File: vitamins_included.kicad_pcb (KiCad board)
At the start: 2 copper layers, 230.5 x 82 mm, 130 parts, among them J1 Speaker, J3 ISP, J5 Speaker, J6 ISP, J7 WS2812>, J8 WS2812>, P2 UJ2-MBH-1-SMT, P3 >WS2812, P4 SJ-43514-SMT, P5 UJ2-MBH-1-SMT, P6 >WS2812, P8 SJ-43514-SMT, SW1 Socket, SW10 Socket, SW11 Socket, SW12 Socket, SW13 Socket, SW14 Socket, SW15 Socket, SW16 Socket, SW17 Socket, SW18 Socket, SW19 Socket, SW2 Socket, SW20 Socket, SW21 Socket, SW22 Socket, SW23 Socket, SW24 Socket, SW24 Socket-overlap, SW25 Socket, SW26 Socket, SW27 Socket, SW28 Socket, SW29 Socket, SW3 Socket, SW30 Socket, SW31 Socket, SW32 Socket, SW33 Socket, SW34 Socket, SW35 Socket, SW36 Socket, SW37 Socket, SW38 Socket, SW39 Socket, SW4 Socket, SW40 Socket, SW41 Socket, SW42 Socket, SW43 Socket, SW43 Socket-overlap, SW44 Socket, SW45 Socket, SW46 Socket, SW47 Socket, SW48 Socket, SW5 Socket, SW6 Socket, SW7 Socket, SW8 Socket, SW9 Socket, U1 ATMega32U4, U2 ATMega32U4, Y1 16MHz, Y2 16MHz

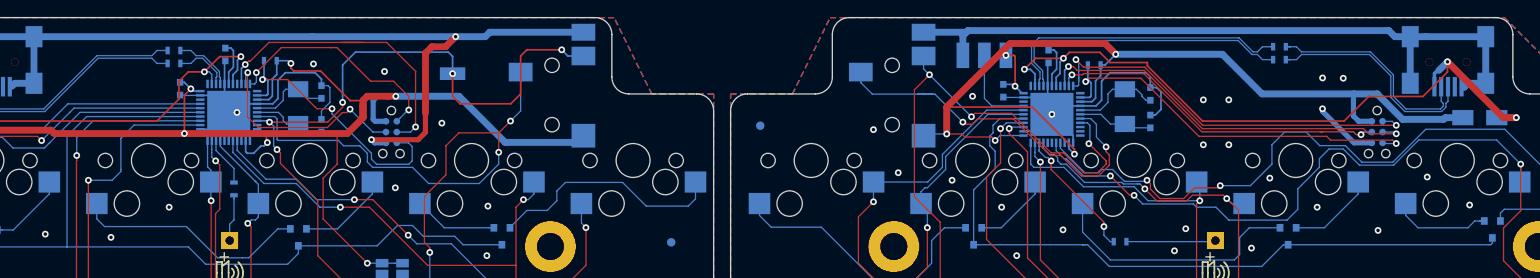
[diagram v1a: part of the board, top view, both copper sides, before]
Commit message: Added resistors to allow MCU to determin which half it is on
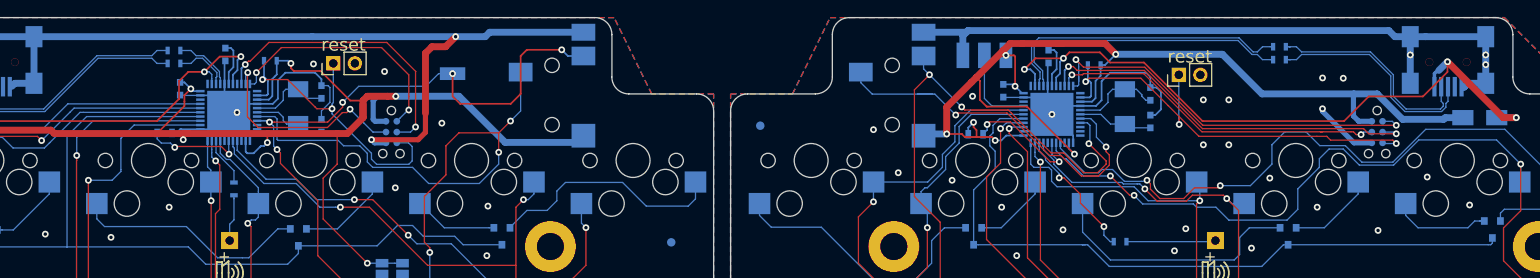
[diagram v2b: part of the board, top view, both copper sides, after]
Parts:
- added J2: reset, Connector_PinHeader_2.54mm:PinHeader_1x02_P2.54mm_Vertical, F.Cu at (69.4, 5.40)
- added J4: reset, Connector_PinHeader_2.54mm:PinHeader_1x02_P2.54mm_Vertical, F.Cu at (169.1, 6.75)
- added R11: 4k7, Resistor_SMD:R_0603_1608Metric, B.Cu at (49.5, 13.6)
- added R12: 4k7, Resistor_SMD:R_0603_1608Metric, B.Cu at (145.2, 13.8)
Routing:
- net Net-(R12-Pad1): track 0.00 -> 14.5 mm, vias 0 -> 2
- net Net-(R11-Pad1): track 0.00 -> 11.6 mm, vias 0 -> 2
- net /Right half/~RESET: track 47.5 -> 54.2 mm, vias 2 -> 3
- net /Left half/SDA: track 84.7 -> 78.8 mm
- net /Left half/~Reset: track 32.3 -> 37.7 mm
- net GND: track 302.5 -> 306.0 mm, vias 50 -> 53
- net /Left half/MISO: track 27.2 -> 28.7 mm
- net VCC: track 306.9 -> 305.7 mm, vias 14 -> 15
- net /Right half/col1: track 76.5 -> 77.6 mm
- net /Right half/col0: track 98.8 -> 99.9 mm
- net /Right half/col2: track 91.6 -> 92.3 mm
- net /Right half/buzz: track 16.6 -> 16.0 mm

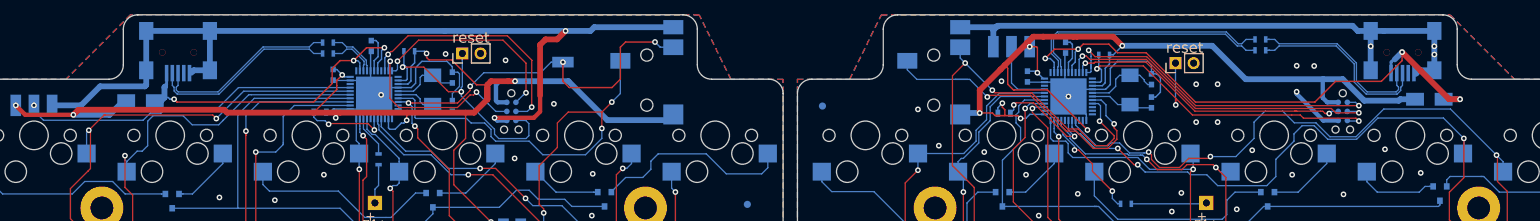
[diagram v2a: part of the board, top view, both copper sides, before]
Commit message: Changed to USB-C connector
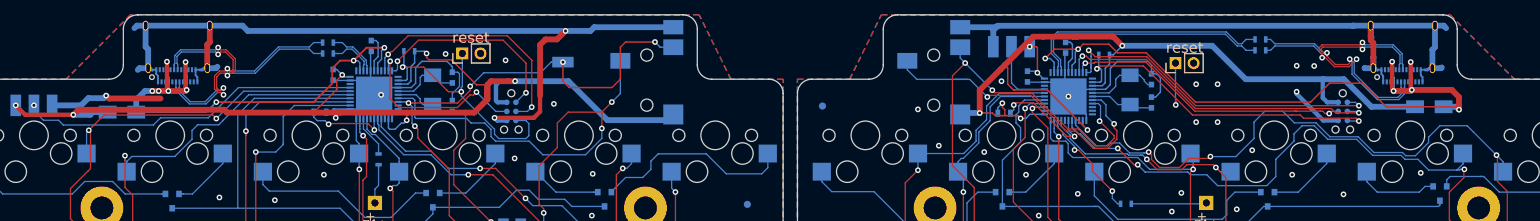
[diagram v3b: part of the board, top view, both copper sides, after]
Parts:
- removed P2, P5: UJ2-MBH-1-SMT, Connectors:USB-Mini-B-SMD
- added J10: 12401598E4#2A, Connector_USB:USB_C_Receptacle_Amphenol_12401610E4-2A, B.Cu at (200.9, 4.35)
- added J9: 12401598E4#2A, Connector_USB:USB_C_Receptacle_Amphenol_12401610E4-2A, B.Cu at (29.6, 4.35)
- R3: value 200R -> 220R
- moved D25 3.05 mm to (21.8, 13.6)
- moved D26 1.05 mm to (204.6, 12.8)
- moved G*** 0.40 mm to (44.1, 6.75)
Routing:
- net VBUS: track 127.6 -> 173.5 mm, vias 7 -> 16
- net GND: track 306.0 -> 328.4 mm, vias 53 -> 50
- net /Left half/Dd+: track 25.9 -> 43.2 mm, vias 0 -> 3
- net /Right half/Dd+: track 26.3 -> 43.3 mm, vias 0 -> 3
- net /Left half/Dd-: track 26.4 -> 43.2 mm, vias 0 -> 3
- net /Right half/Dd-: track 25.8 -> 42.3 mm, vias 0 -> 3
- net /Right half/col4: track 139.7 -> 135.5 mm
- net VCC: track 305.7 -> 302.7 mm
- net /Left half/col1: track 108.2 -> 105.9 mm
- net /Right half/col5: track 140.3 -> 141.0 mm
- net /Left half/wd2812-in: track 47.4 -> 48.0 mm

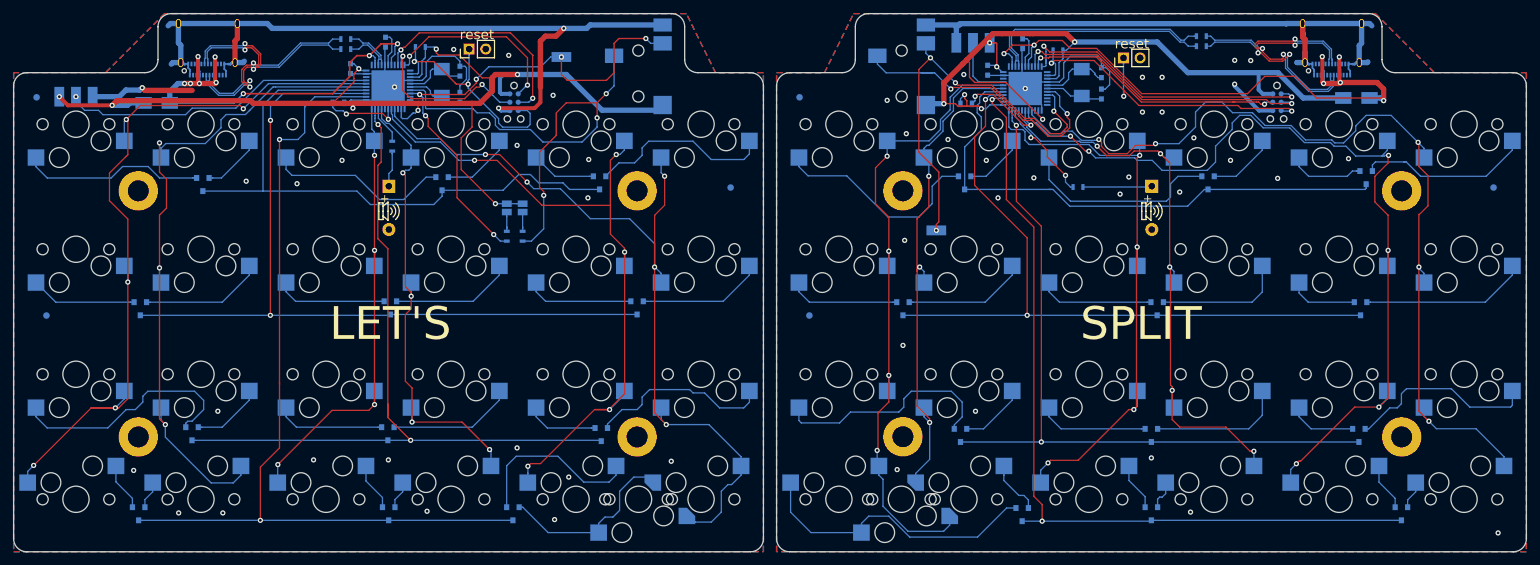
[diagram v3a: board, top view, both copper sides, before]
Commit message: Added resistors to allow the firmware to determine version
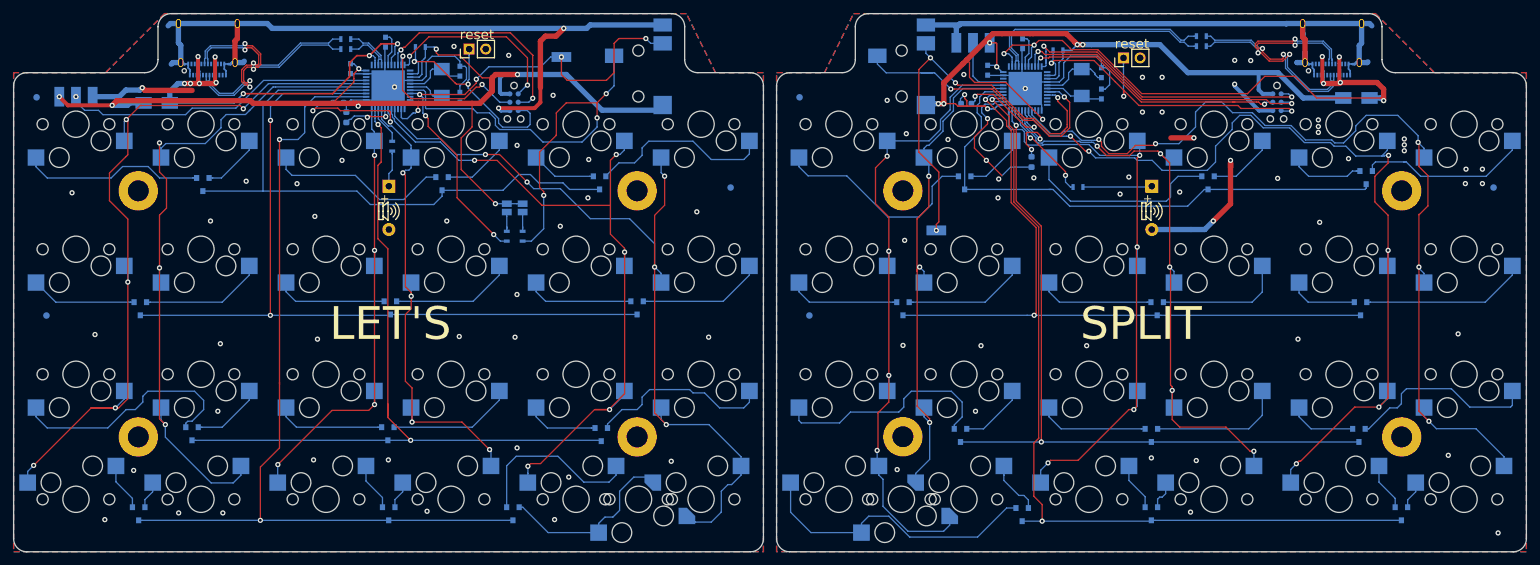
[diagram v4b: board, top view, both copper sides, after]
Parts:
- added R13: 4k7, Resistor_SMD:R_0603_1608Metric, B.Cu at (50.7, 15.8)
- added R14: 4k7, Resistor_SMD:R_0603_1608Metric, B.Cu at (155.1, 22.6)
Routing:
- net GND: track 328.4 -> 376.2 mm, vias 50 -> 86
- net Net-(R14-Pad1): track 0.00 -> 12.3 mm, vias 0 -> 2
- net Net-(R13-Pad1): track 0.00 -> 7.85 mm, vias 0 -> 2
- net Net-(R11-Pad1): track 11.6 -> 19.4 mm
- net /Right half/SCL/D3: track 45.2 -> 46.6 mm
- net Net-(R12-Pad1): track 14.5 -> 15.9 mm
- net VCC: track 302.7 -> 303.5 mm, vias 15 -> 17
- net /Right half/row1: track 109.6 -> 108.9 mm
- net /Right half/col3: track 91.3 -> 92.0 mm
- net /Right half/row3: track 127.0 -> 127.6 mm
- net /Right half/col5: track 141.0 -> 141.6 mm
- net (no net): vias 3 -> 1

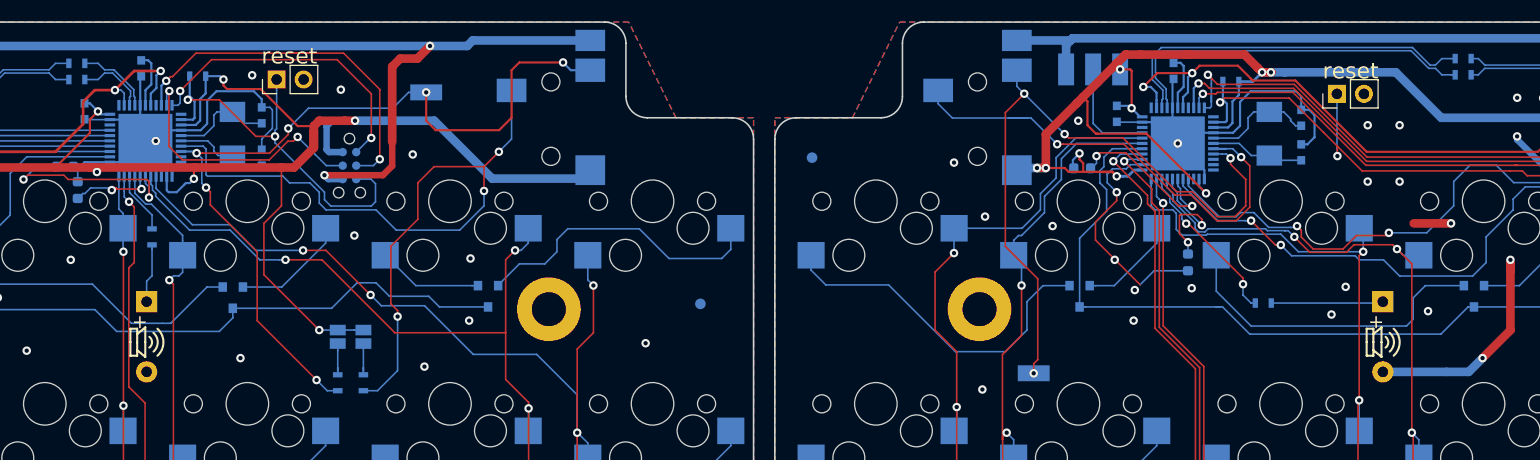
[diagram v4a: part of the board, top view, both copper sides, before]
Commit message: changed to rounded passive footprints
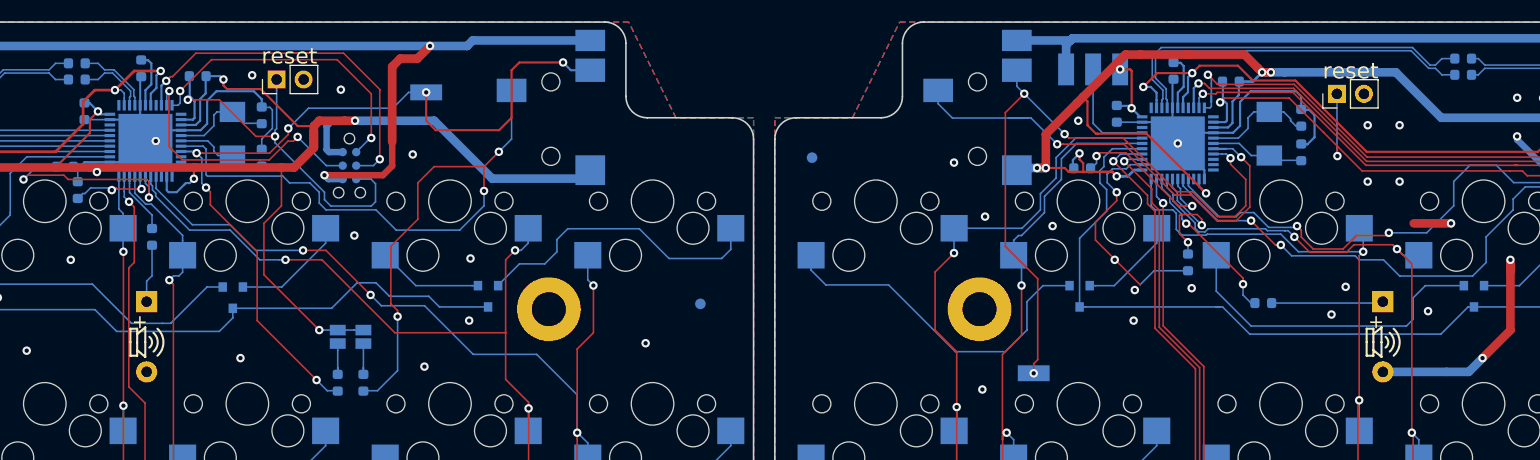
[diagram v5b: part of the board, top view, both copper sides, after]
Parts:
- C1, C2, C3, C4, C5, C6, C7, C8: footprint Capacitors_SMD:C_0603 -> Capacitor_SMD:C_0603_1608Metric
- R1, R2, R3, R4, R5, R6, R7, R8, R9: footprint Resistors_SMD:R_0603 -> Resistor_SMD:R_0603_1608Metric
- R10: value 200R -> 220R; footprint Resistors_SMD:R_0603 -> Resistor_SMD:R_0603_1608Metric
- R11, R12, R13, R14: value 4k7 -> 220R
- SW24, SW43: value Socket-overlap -> Socket
